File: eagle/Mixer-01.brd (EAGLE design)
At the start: 95 x 72 mm, 58 parts, among them IC1 TL072P, IC2 TL072P, IC3 LM4558N

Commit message: Mixer-01.brd 結線を修正
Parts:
- C10: value 0.2u -> 0.1u
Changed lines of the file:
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@@
 <attribute name="VALUE" x="46.609" y="33.147" size="1.27" layer="27" ratio="10" rot="R180"/>
 </element>
-<element name="C10" library="resistor" package="C050-024X044" value="0.2u" x="45.72" y="17.78" smashed="yes" rot="R180">
+<element name="C10" library="resistor" package="C050-024X044" value="0.1u" x="45.72" y="17.78" smashed="yes" rot="R180">
 <attribute name="NAME" x="42.799" y="16.383" size="1.27" layer="25" ratio="10" rot="R180"/>
 <attribute name="VALUE" x="42.799" y="17.907" size="1.27" layer="27" ratio="10" rot="R180"/>

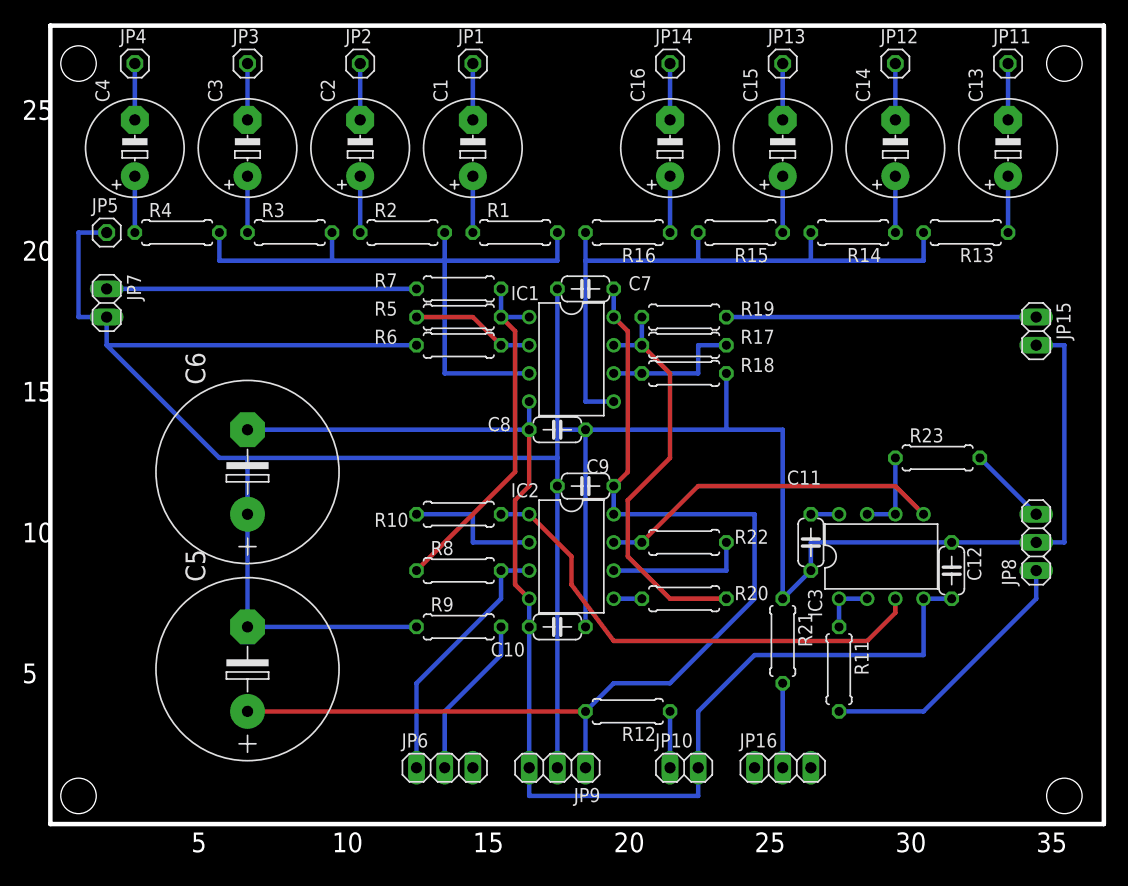
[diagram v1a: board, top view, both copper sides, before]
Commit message: Mixer-01.brd: ICを水平に
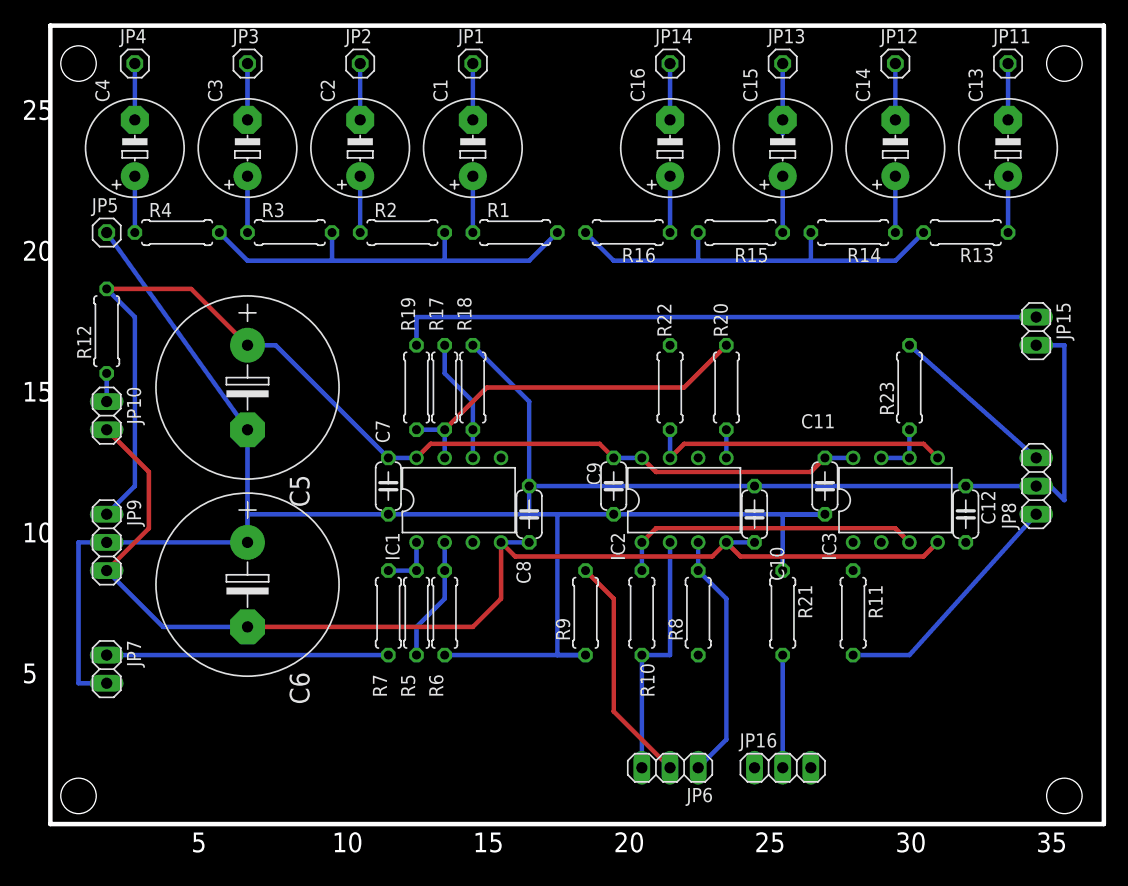
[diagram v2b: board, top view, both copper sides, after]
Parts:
- moved JP10 61.0 mm to (5.08, 36.8), turned to 270 degrees
- moved R12 58.2 mm to (5.08, 44.5), turned to 90 degrees
- moved JP9 45.4 mm to (5.08, 25.4), turned to 270 degrees
- moved JP7 33.0 mm to (5.08, 14.0)
- moved R7 29.9 mm to (30.5, 19.1), turned to 270 degrees
- moved R5 26.9 mm to (33.0, 19.1), turned to 90 degrees
- moved C5 25.4 mm to (17.8, 39.4), turned to 270 degrees
- moved C7 25.1 mm to (30.5, 30.5), turned to 270 degrees
- moved R19 25.0 mm to (33.0, 39.4), turned to 90 degrees
- moved R6 24.2 mm to (35.6, 19.1), turned to 90 degrees
- moved R8 21.9 mm to (58.4, 19.1), turned to 90 degrees
- moved R17 21.9 mm to (35.6, 39.4), turned to 270 degrees
- moved C10 20.5 mm to (63.5, 27.9), turned to 270 degrees
- moved JP6 20.3 mm to (55.9, 5.08), turned to 180 degrees
- moved R20 19.4 mm to (61.0, 39.4), turned to 270 degrees
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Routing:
- net GND: track 269.4 -> 234.0 mm
- net N$27: track 29.2 -> 58.4 mm
- net N$15: track 32.1 -> 5.08 mm
- net N$13: track 58.4 -> 37.7 mm
- net N$24: track 55.9 -> 37.7 mm
- net N$20: track 44.5 -> 27.7 mm
- net N$29: track 12.7 -> 0.00 mm
- net N$19: track 12.7 -> 22.9 mm
- net V-: track 114.9 -> 106.2 mm
- net N$32: track 7.18 -> 15.3 mm
- net N$6: track 14.8 -> 20.9 mm
- net N$21: track 5.08 -> 0.00 mm
- net N$26: track 37.2 -> 33.6 mm
- net N$30: track 31.1 -> 27.7 mm
- net N$31: track 7.62 -> 5.08 mm
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
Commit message: Mixer-01.brd: 修正
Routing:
- net N$13: track 37.7 -> 69.8 mm
- net N$29: track 0.00 -> 12.7 mm
- net GND: track 234.0 -> 242.9 mm
- net N$21: track 0.00 -> 5.08 mm
- net V-: track 106.2 -> 108.7 mm
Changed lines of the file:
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@@
 <layer number="97" name="Info" color="7" fill="1" visible="no" active="no"/>
 <layer number="98" name="Guide" color="6" fill="1" visible="no" active="no"/>
-<layer number="100" name="Grid" color="7" fill="1" visible="yes" active="yes"/>
+<layer number="100" name="Grid" color="7" fill="1" visible="no" active="yes"/>
 <layer number="101" name="Jumper" color="14" fill="1" visible="yes" active="yes"/>
 </layers>
@@
 <wire x1="93.98" y1="0" x2="93.98" y2="72.39" width="0.0254" layer="100"/>
 <wire x1="7.62" y1="71.12" x2="7.62" y2="72.39" width="0.0254" layer="100"/>
-<wire x1="35.56" y1="50.8" x2="38.1" y2="25.4" width="0.4064" layer="101"/>
 <wire x1="40.64" y1="33.02" x2="50.8" y2="50.8" width="0.4064" layer="101"/>
-<wire x1="55.88" y1="43.18" x2="58.42" y2="33.02" width="0.4064" layer="101"/>
 <wire x1="58.42" y1="33.02" x2="68.58" y2="5.08" width="0.4064" layer="101"/>
 <wire x1="60.96" y1="33.02" x2="63.5" y2="5.08" width="0.4064" layer="101"/>
@@
 <wire x1="62.23" y1="24.13" x2="60.96" y2="25.4" width="0.4064" layer="1"/>
 <wire x1="63.5" y1="25.4" x2="60.96" y2="25.4" width="0.4064" layer="16"/>
-<wire x1="80.01" y1="25.4" x2="82.55" y2="25.4" width="0" layer="19" extent="1-1"/>
+<wire x1="80.01" y1="25.4" x2="82.55" y2="25.4" width="0.4064" layer="16"/>
 </signal>
 <signal name="GND">
@@
 <wire x1="30.48" y1="27.94" x2="17.78" y2="27.94" width="0.4064" layer="16"/>
 <wire x1="50.8" y1="27.94" x2="69.85" y2="27.94" width="0.4064" layer="16"/>
-<wire x1="43.18" y1="30.48" x2="82.55" y2="30.48" width="0.4064" layer="16"/>
+<wire x1="43.18" y1="30.48" x2="63.5" y2="30.48" width="0.4064" layer="16"/>
+<wire x1="63.5" y1="30.48" x2="82.55" y2="30.48" width="0.4064" layer="16"/>
 <wire x1="82.55" y1="30.48" x2="88.9" y2="30.48" width="0.4064" layer="16"/>
 <wire x1="17.78" y1="25.4" x2="5.08" y2="25.4" width="0.4064" layer="16"/>
@@
 <wire x1="38.1" y1="43.18" x2="43.18" y2="38.1" width="0.4064" layer="16"/>
 <wire x1="43.18" y1="38.1" x2="43.18" y2="30.48" width="0.4064" layer="16"/>
-<wire x1="66.04" y1="27.94" x2="63.5" y2="30.48" width="0" layer="19" extent="16-16"/>
+<wire x1="63.5" y1="30.48" x2="69.85" y2="30.48" width="0.4064" layer="16"/>
+<wire x1="69.85" y1="30.48" x2="69.85" y2="27.94" width="0.4064" layer="16"/>
 </signal>
 <signal name="N$9">
@@
 <wire x1="35.56" y1="53.34" x2="35.56" y2="50.8" width="0.4064" layer="16"/>
 <wire x1="25.4" y1="53.34" x2="25.4" y2="50.8" width="0.4064" layer="16"/>
-<wire x1="38.1" y1="25.4" x2="35.56" y2="50.8" width="0" layer="19" extent="16-16"/>
+<wire x1="38.1" y1="25.4" x2="31.75" y2="31.75" width="0.4064" layer="1"/>
+<wire x1="35.56" y1="53.34" x2="31.75" y2="49.53" width="0.4064" layer="1"/>
+<wire x1="31.75" y1="49.53" x2="31.75" y2="31.75" width="0.4064" layer="1"/>
 </signal>
 <signal name="N$14">
@@
 <contactref element="IC3" pad="1"/>
 <contactref element="R11" pad="1"/>
-<wire x1="72.39" y1="25.4" x2="74.93" y2="25.4" width="0" layer="19" extent="1-1"/>
-<wire x1="72.39" y1="22.86" x2="72.39" y2="25.4" width="0" layer="19" extent="1-1"/>
+<wire x1="74.93" y1="25.4" x2="72.39" y2="25.4" width="0.4064" layer="16"/>
+<wire x1="72.39" y1="25.4" x2="72.39" y2="22.86" width="0.4064" layer="16"/>
 </signal>
 <signal name="N$22">
@@
 <contactref element="JP16" pad="3"/>
 <contactref element="IC2" pad="6"/>
-<wire x1="58.42" y1="33.02" x2="55.88" y2="43.18" width="0" layer="19" extent="1-1"/>
 <wire x1="68.58" y1="5.08" x2="58.42" y2="33.02" width="0" layer="19" extent="1-1"/>
+<wire x1="55.88" y1="43.18" x2="58.42" y2="43.18" width="0.4064" layer="16"/>
+<wire x1="58.42" y1="43.18" x2="58.42" y2="33.02" width="0.4064" layer="16"/>
 </signal>
 <signal name="N$30">
